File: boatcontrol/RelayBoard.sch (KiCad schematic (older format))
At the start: 15 parts, among them J2301 Conn_02x20_Odd_Even Header, J2302 TBL008V-1000-08BE, J2303 TBL008V-1000-08BE, K2301 EW60-1A3-CL12D04, K2302 EW60-1A3-CL12D04, K2303 EW60-1A3-CL12D04, K2304 EW60-1A3-CL12D04, K2305 EW60-1A3-CL12D04, K2306 EW60-1A3-CL12D04, K2307 EW60-1A3-CL12D04, K2308 EW60-1A3-CL12D04

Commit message: Organize more
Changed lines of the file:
@@
 AR Path="/E0EE2714/E107FCD3/E1098DA6" Ref="#PWR?"  Part="1"
 AR Path="/E171B338/E1098DA6" Ref="#PWR02301"  Part="1"
-AR Path="/E171B33C/5F80BAC6/E1098DA6" Ref="#PWR?"  Part="1"
-F 0 "#PWR?" H 3200 3800 50  0001 C CNN
+AR Path="/E171B33C/5F80BAC6/E1098DA6" Ref="#PWR0107"  Part="1"
+F 0 "#PWR0107" H 3200 3800 50  0001 C CNN
 F 1 "GND" H 3400 4050 50  0000 R CNN
 F 2 "" H 3200 4050 50  0001 C CNN
@@
 AR Path="/E0EE2714/E107FCD3/E1098DAC" Ref="#PWR?"  Part="1"
 AR Path="/E171B338/E1098DAC" Ref="#PWR02302"  Part="1"
-AR Path="/E171B33C/5F80BAC6/E1098DAC" Ref="#PWR?"  Part="1"
-F 0 "#PWR?" H 4250 3800 50  0001 C CNN
+AR Path="/E171B33C/5F80BAC6/E1098DAC" Ref="#PWR0123"  Part="1"
+F 0 "#PWR0123" H 4250 3800 50  0001 C CNN
 F 1 "GND" H 4450 4050 50  0000 R CNN
 F 2 "" H 4250 4050 50  0001 C CNN
@@
 AR Path="/E0EE2714/E107FCD3/E1098DB2" Ref="#PWR?"  Part="1"
 AR Path="/E171B338/E1098DB2" Ref="#PWR02303"  Part="1"
-AR Path="/E171B33C/5F80BAC6/E1098DB2" Ref="#PWR?"  Part="1"
-F 0 "#PWR?" H 5300 3800 50  0001 C CNN
+AR Path="/E171B33C/5F80BAC6/E1098DB2" Ref="#PWR0124"  Part="1"
+F 0 "#PWR0124" H 5300 3800 50  0001 C CNN
 F 1 "GND" H 5500 4050 50  0000 R CNN
 F 2 "" H 5300 4050 50  0001 C CNN
@@
 AR Path="/E0EE2714/E107FCD3/E1098DB8" Ref="#PWR?"  Part="1"
 AR Path="/E171B338/E1098DB8" Ref="#PWR02304"  Part="1"
-AR Path="/E171B33C/5F80BAC6/E1098DB8" Ref="#PWR?"  Part="1"
-F 0 "#PWR?" H 6350 3800 50  0001 C CNN
+AR Path="/E171B33C/5F80BAC6/E1098DB8" Ref="#PWR0125"  Part="1"
+F 0 "#PWR0125" H 6350 3800 50  0001 C CNN
 F 1 "GND" H 6550 4050 50  0000 R CNN
 F 2 "" H 6350 4050 50  0001 C CNN
@@
 AR Path="/E0EE2714/E107FCD3/E1098DC4" Ref="#PWR?"  Part="1"
 AR Path="/E171B338/E1098DC4" Ref="#PWR02306"  Part="1"
-AR Path="/E171B33C/5F80BAC6/E1098DC4" Ref="#PWR?"  Part="1"
-F 0 "#PWR?" H 8450 3800 50  0001 C CNN
+AR Path="/E171B33C/5F80BAC6/E1098DC4" Ref="#PWR0126"  Part="1"
+F 0 "#PWR0126" H 8450 3800 50  0001 C CNN
 F 1 "GND" H 8650 4050 50  0000 R CNN
 F 2 "" H 8450 4050 50  0001 C CNN
@@
 AR Path="/E0EE2714/E107FCD3/E1098DCA" Ref="#PWR?"  Part="1"
 AR Path="/E171B338/E1098DCA" Ref="#PWR02307"  Part="1"
-AR Path="/E171B33C/5F80BAC6/E1098DCA" Ref="#PWR?"  Part="1"
-F 0 "#PWR?" H 9500 3800 50  0001 C CNN
+AR Path="/E171B33C/5F80BAC6/E1098DCA" Ref="#PWR0127"  Part="1"
+F 0 "#PWR0127" H 9500 3800 50  0001 C CNN
 F 1 "GND" H 9700 4050 50  0000 R CNN
 F 2 "" H 9500 4050 50  0001 C CNN
@@
 AR Path="/E0EE2714/E107FCD3/E1098DD0" Ref="#PWR?"  Part="1"
 AR Path="/E171B338/E1098DD0" Ref="#PWR02308"  Part="1"
-AR Path="/E171B33C/5F80BAC6/E1098DD0" Ref="#PWR?"  Part="1"
-F 0 "#PWR?" H 10550 3800 50  0001 C CNN
+AR Path="/E171B33C/5F80BAC6/E1098DD0" Ref="#PWR0128"  Part="1"
+F 0 "#PWR0128" H 10550 3800 50  0001 C CNN
 F 1 "GND" H 10750 4050 50  0000 R CNN
 F 2 "" H 10550 4050 50  0001 C CNN
@@
 AR Path="/E0EE2714/E107FCD3/E1098DD9" Ref="J?"  Part="1"
 AR Path="/E171B338/E1098DD9" Ref="J2303"  Part="1"
-AR Path="/E171B33C/5F80BAC6/E1098DD9" Ref="J?"  Part="1"
-F 0 "J?" V 7146 4922 50  0000 R CNN
+AR Path="/E171B33C/5F80BAC6/E1098DD9" Ref="J3403"  Part="1"
+F 0 "J3403" V 7146 4922 50  0000 R CNN
 F 1 "TBL008V-1000-08BE" V 7400 5800 50  0000 R CNN
 F 2 "CUI_TBL008V-1000-08BE" H 7300 5350 50  0001 L BNN
@@
 AR Path="/E0EE2714/E107FCD3/E1098DE2" Ref="J?"  Part="1"
 AR Path="/E171B338/E1098DE2" Ref="J2302"  Part="1"
-AR Path="/E171B33C/5F80BAC6/E1098DE2" Ref="J?"  Part="1"
-F 0 "J?" V 7146 2372 50  0000 R CNN
+AR Path="/E171B33C/5F80BAC6/E1098DE2" Ref="J3402"  Part="1"
+F 0 "J3402" V 7146 2372 50  0000 R CNN
 F 1 "TBL008V-1000-08BE" V 7400 3250 50  0000 R CNN
 F 2 "CUI_TBL008V-1000-08BE" H 7300 2800 50  0001 L BNN
@@
 AR Path="/E0EE2714/E107FCD3/E1098DE8" Ref="K?"  Part="1"
 AR Path="/E171B338/E1098DE8" Ref="K2302"  Part="1"
-AR Path="/E171B33C/5F80BAC6/E1098DE8" Ref="K?"  Part="1"
-F 0 "K?" V 4800 3850 50  0000 L CNN
+AR Path="/E171B33C/5F80BAC6/E1098DE8" Ref="K3402"  Part="1"
+F 0 "K3402" V 4800 3850 50  0000 L CNN
 F 1 "EW60-1A3-CL12D04" V 4550 3600 50  0000 L CNN
 F 2 "BoatControl:TE_2071366-2" H 4750 4400 50  0001 L BNN
@@
 AR Path="/E0EE2714/E107FCD3/E1098DEE" Ref="K?"  Part="1"
 AR Path="/E171B338/E1098DEE" Ref="K2303"  Part="1"
-AR Path="/E171B33C/5F80BAC6/E1098DEE" Ref="K?"  Part="1"
-F 0 "K?" V 5850 3850 50  0000 L CNN
+AR Path="/E171B33C/5F80BAC6/E1098DEE" Ref="K3403"  Part="1"
+F 0 "K3403" V 5850 3850 50  0000 L CNN
 F 1 "EW60-1A3-CL12D04" V 5600 3600 50  0000 L CNN
 F 2 "BoatControl:TE_2071366-2" H 5800 4400 50  0001 L BNN
@@
 AR Path="/E0EE2714/E107FCD3/E1098DF4" Ref="K?"  Part="1"
 AR Path="/E171B338/E1098DF4" Ref="K2304"  Part="1"
-AR Path="/E171B33C/5F80BAC6/E1098DF4" Ref="K?"  Part="1"
-F 0 "K?" V 6900 3850 50  0000 L CNN
+AR Path="/E171B33C/5F80BAC6/E1098DF4" Ref="K3404"  Part="1"
+F 0 "K3404" V 6900 3850 50  0000 L CNN
 F 1 "EW60-1A3-CL12D04" V 6650 3600 50  0000 L CNN
 F 2 "BoatControl:TE_2071366-2" H 6850 4400 50  0001 L BNN
@@
 AR Path="/E0EE2714/E107FCD3/E1098DFA" Ref="K?"  Part="1"
 AR Path="/E171B338/E1098DFA" Ref="K2305"  Part="1"
-AR Path="/E171B33C/5F80BAC6/E1098DFA" Ref="K?"  Part="1"
-F 0 "K?" V 7950 3850 50  0000 L CNN
+AR Path="/E171B33C/5F80BAC6/E1098DFA" Ref="K3405"  Part="1"
+F 0 "K3405" V 7950 3850 50  0000 L CNN
 F 1 "EW60-1A3-CL12D04" V 7700 3600 50  0000 L CNN
 F 2 "BoatControl:TE_2071366-2" H 7900 4400 50  0001 L BNN
@@
 AR Path="/E0EE2714/E107FCD3/E1098E00" Ref="K?"  Part="1"
 AR Path="/E171B338/E1098E00" Ref="K2306"  Part="1"
-AR Path="/E171B33C/5F80BAC6/E1098E00" Ref="K?"  Part="1"
-F 0 "K?" V 9000 3850 50  0000 L CNN
+AR Path="/E171B33C/5F80BAC6/E1098E00" Ref="K3406"  Part="1"
+F 0 "K3406" V 9000 3850 50  0000 L CNN
 F 1 "EW60-1A3-CL12D04" V 8750 3600 50  0000 L CNN
 F 2 "BoatControl:TE_2071366-2" H 8950 4400 50  0001 L BNN
@@
 AR Path="/E0EE2714/E107FCD3/E1098E06" Ref="K?"  Part="1"
 AR Path="/E171B338/E1098E06" Ref="K2307"  Part="1"
-AR Path="/E171B33C/5F80BAC6/E1098E06" Ref="K?"  Part="1"
-F 0 "K?" V 10050 3850 50  0000 L CNN
+AR Path="/E171B33C/5F80BAC6/E1098E06" Ref="K3407"  Part="1"
+F 0 "K3407" V 10050 3850 50  0000 L CNN
 F 1 "EW60-1A3-CL12D04" V 9800 3600 50  0000 L CNN
 F 2 "BoatControl:TE_2071366-2" H 10000 4400 50  0001 L BNN
@@
 AR Path="/E0EE2714/E107FCD3/E1098E0C" Ref="K?"  Part="1"
 AR Path="/E171B338/E1098E0C" Ref="K2308"  Part="1"
-AR Path="/E171B33C/5F80BAC6/E1098E0C" Ref="K?"  Part="1"
-F 0 "K?" V 11100 3850 50  0000 L CNN
+AR Path="/E171B33C/5F80BAC6/E1098E0C" Ref="K3408"  Part="1"
+F 0 "K3408" V 11100 3850 50  0000 L CNN
 F 1 "EW60-1A3-CL12D04" V 10850 3550 50  0000 L CNN
 F 2 "BoatControl:TE_2071366-2" H 11050 4400 50  0001 L BNN
@@
 AR Path="/E0EE2714/E107FCD3/E1098E6E" Ref="J?"  Part="1"
 AR Path="/E171B338/E1098E6E" Ref="J2301"  Part="1"
-AR Path="/E171B33C/5F80BAC6/E1098E6E" Ref="J?"  Part="1"
-F 0 "J?" V 1346 2913 50  0000 R CNN
+AR Path="/E171B33C/5F80BAC6/E1098E6E" Ref="J3401"  Part="1"
+F 0 "J3401" V 1346 2913 50  0000 R CNN
 F 1 "Conn_02x20_Odd_Even Header" V 1300 4450 50  0000 R CNN
 F 2 "Connector_PinSocket_2.54mm:PinSocket_2x20_P2.54mm_Vertical" H 1250 4000 50  0001 C CNN
@@
 AR Path="/E0EE2714/E107FCD3/E1098E74" Ref="H?"  Part="1"
 AR Path="/E171B338/E1098E74" Ref="H2301"  Part="1"
-AR Path="/E171B33C/5F80BAC6/E1098E74" Ref="H?"  Part="1"
-F 0 "H?" H 150 3946 50  0000 L CNN
+AR Path="/E171B33C/5F80BAC6/E1098E74" Ref="H3401"  Part="1"
+F 0 "H3401" H 150 3946 50  0000 L CNN
 F 1 "MountingHole" H 150 3855 50  0000 L CNN
 F 2 "MountingHole:MountingHole_3mm" H 50  3900 50  0001 C CNN
@@
 AR Path="/E0EE2714/E107FCD3/E1098E7A" Ref="H?"  Part="1"
 AR Path="/E171B338/E1098E7A" Ref="H2302"  Part="1"
-AR Path="/E171B33C/5F80BAC6/E1098E7A" Ref="H?"  Part="1"
-F 0 "H?" H 150 4296 50  0000 L CNN
+AR Path="/E171B33C/5F80BAC6/E1098E7A" Ref="H3402"  Part="1"
+F 0 "H3402" H 150 4296 50  0000 L CNN
 F 1 "MountingHole" H 150 4205 50  0000 L CNN
 F 2 "MountingHole:MountingHole_3mm" H 50  4250 50  0001 C CNN
@@
 AR Path="/E0EE2714/E107FCD3/E1098E80" Ref="H?"  Part="1"
 AR Path="/E171B338/E1098E80" Ref="H2304"  Part="1"
-AR Path="/E171B33C/5F80BAC6/E1098E80" Ref="H?"  Part="1"
-F 0 "H?" H 2450 4296 50  0000 L CNN
+AR Path="/E171B33C/5F80BAC6/E1098E80" Ref="H3404"  Part="1"
+F 0 "H3404" H 2450 4296 50  0000 L CNN
 F 1 "MountingHole" H 2450 4205 50  0000 L CNN
 F 2 "MountingHole:MountingHole_3mm" H 2350 4250 50  0001 C CNN
@@
 AR Path="/E0EE2714/E107FCD3/E1098E86" Ref="H?"  Part="1"
 AR Path="/E171B338/E1098E86" Ref="H2303"  Part="1"
-AR Path="/E171B33C/5F80BAC6/E1098E86" Ref="H?"  Part="1"
-F 0 "H?" H 2450 3946 50  0000 L CNN
+AR Path="/E171B33C/5F80BAC6/E1098E86" Ref="H3403"  Part="1"
+F 0 "H3403" H 2450 3946 50  0000 L CNN
 F 1 "MountingHole" H 2450 3855 50  0000 L CNN
 F 2 "MountingHole:MountingHole_3mm" H 2350 3900 50  0001 C CNN
@@
 AR Path="/E0EE2714/E107FCD3/E1098E92" Ref="K?"  Part="1"
 AR Path="/E171B338/E1098E92" Ref="K2301"  Part="1"
-AR Path="/E171B33C/5F80BAC6/E1098E92" Ref="K?"  Part="1"
-F 0 "K?" V 3750 3850 50  0000 L CNN
+AR Path="/E171B33C/5F80BAC6/E1098E92" Ref="K3401"  Part="1"
+F 0 "K3401" V 3750 3850 50  0000 L CNN
 F 1 "EW60-1A3-CL12D04" V 3500 3600 50  0000 L CNN
 F 2 "BoatControl:TE_2071366-2" H 3700 4400 50  0001 L BNN
@@
 AR Path="/E0EE2714/E107FCD3/5F4F4DC8" Ref="#PWR?"  Part="1"
 AR Path="/E171B338/5F4F4DC8" Ref="#PWR02305"  Part="1"
-AR Path="/E171B33C/5F80BAC6/5F4F4DC8" Ref="#PWR?"  Part="1"
-F 0 "#PWR?" H 7400 3800 50  0001 C CNN
+AR Path="/E171B33C/5F80BAC6/5F4F4DC8" Ref="#PWR0129"  Part="1"
+F 0 "#PWR0129" H 7400 3800 50  0001 C CNN
 F 1 "GND" H 7600 4050 50  0000 R CNN
 F 2 "" H 7400 4050 50  0001 C CNN

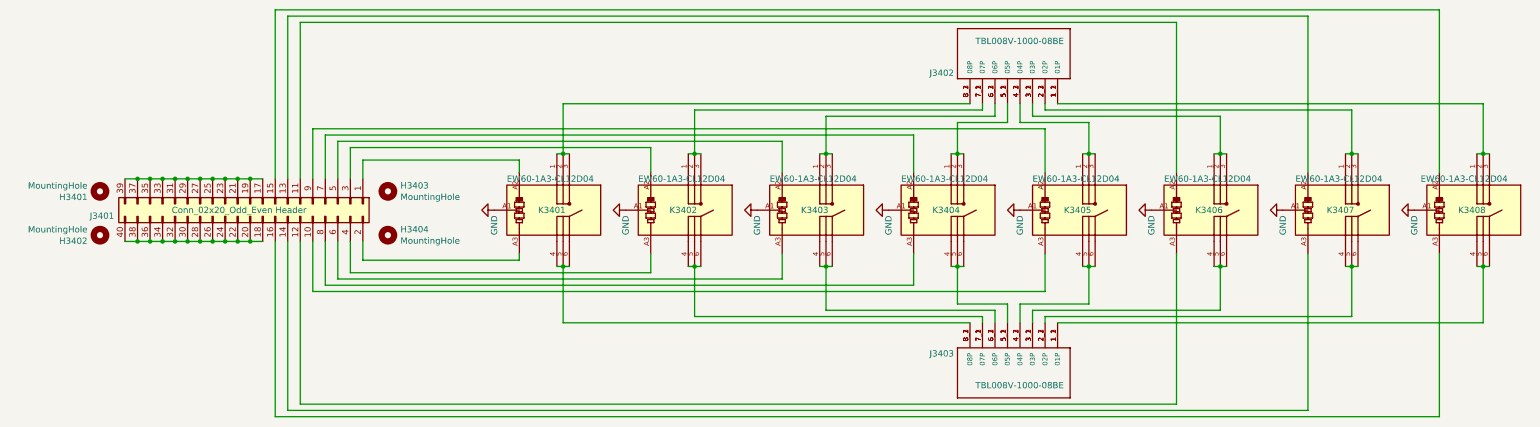
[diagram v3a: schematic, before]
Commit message: Restructure power and daughter boards
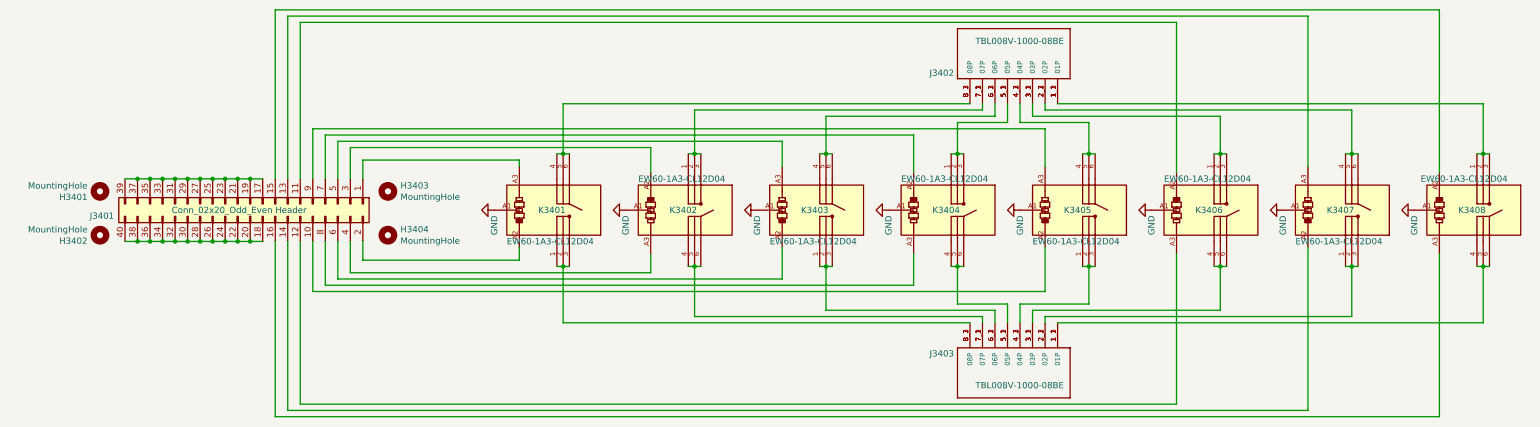
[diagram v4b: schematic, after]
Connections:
- net at J2303.2_1 (02P), J2303.2_2 (02P), J2303.2_3 (02P): now also K2307.1, K2307.2, K2307.3; no longer K2307.4, K2307.5, K2307.6
- net at J2303.4_1 (04P), J2303.4_2 (04P), J2303.4_3 (04P): now also K2305.1, K2305.2, K2305.3; no longer K2305.4, K2305.5, K2305.6
- net at J2303.6_1 (06P), J2303.6_2 (06P), J2303.6_3 (06P): now also K2303.1, K2303.2, K2303.3; no longer K2303.4, K2303.5, K2303.6
- net at J2303.8_1 (08P), J2303.8_2 (08P), J2303.8_3 (08P): now also K2301.1, K2301.2, K2301.3; no longer K2301.4, K2301.5, K2301.6
- net at J2302.2_1 (02P), J2302.2_2 (02P), J2302.2_3 (02P): now also K2307.4, K2307.5, K2307.6; no longer K2307.1, K2307.2, K2307.3
- net at J2302.4_1 (04P), J2302.4_2 (04P), J2302.4_3 (04P): now also K2305.4, K2305.5, K2305.6; no longer K2305.1, K2305.2, K2305.3
- net at J2302.6_1 (06P), J2302.6_2 (06P), J2302.6_3 (06P): now also K2303.4, K2303.5, K2303.6; no longer K2303.1, K2303.2, K2303.3
- net at J2302.8_1 (08P), J2302.8_2 (08P), J2302.8_3 (08P): now also K2301.4, K2301.5, K2301.6; no longer K2301.1, K2301.2, K2301.3
- net at K2303.A2: now also J2301.6 (Pin_6); no longer J2301.5 (Pin_5)
- net at K2303.A3: now also J2301.5 (Pin_5); no longer J2301.6 (Pin_6)
- net at K2305.A2: now also J2301.10 (Pin_10); no longer J2301.9 (Pin_9)
- net at K2305.A3: now also J2301.9 (Pin_9); no longer J2301.10 (Pin_10)
- net at K2307.A2: now also J2301.14 (Pin_14); no longer J2301.13 (Pin_13)
- net at K2307.A3: now also J2301.13 (Pin_13); no longer J2301.14 (Pin_14)
- net at J2301.1 (Pin_1): now also K2301.A3; no longer K2301.A2
- net at J2301.2 (Pin_2): now also K2301.A2; no longer K2301.A3

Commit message: Fixed daughter board
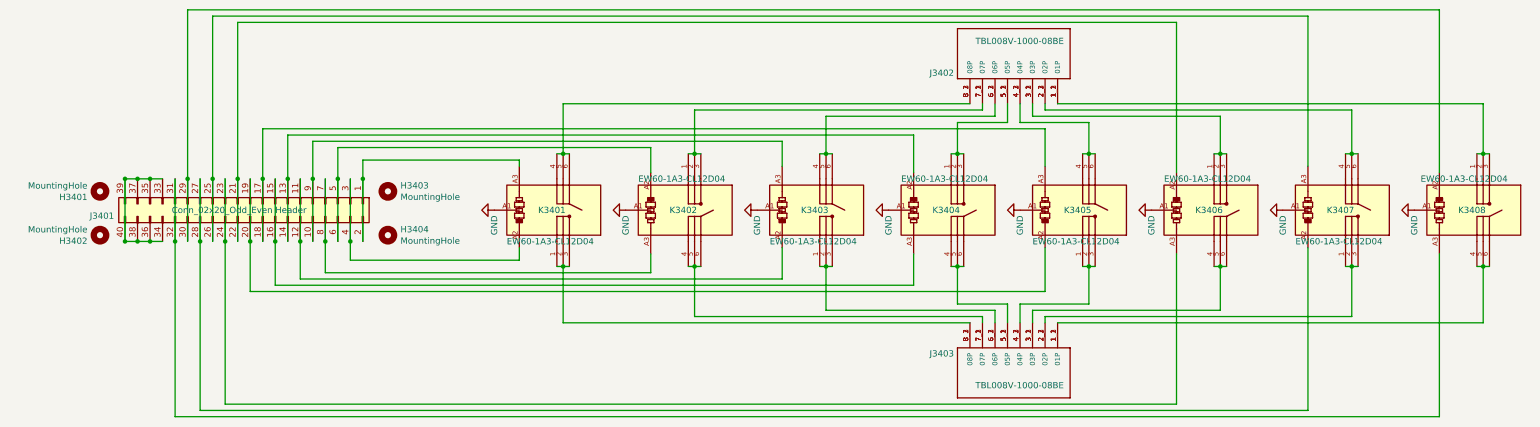
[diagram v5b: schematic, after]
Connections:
- net at K2302.A2: now also J2301.5 (Pin_5), J2301.6 (Pin_6); no longer J2301.3 (Pin_3)
- net at K2302.A3: now also J2301.7 (Pin_7), J2301.8 (Pin_8); no longer J2301.4 (Pin_4)
- net at K2303.A2: now also J2301.11 (Pin_11), J2301.12 (Pin_12); no longer J2301.6 (Pin_6)
- net at K2303.A3: now also J2301.10 (Pin_10), J2301.9 (Pin_9); no longer J2301.5 (Pin_5)
- net at K2304.A2: now also J2301.13 (Pin_13), J2301.14 (Pin_14); no longer J2301.7 (Pin_7)
- net at K2304.A3: now also J2301.15 (Pin_15), J2301.16 (Pin_16); no longer J2301.8 (Pin_8)
- net at K2305.A2: now also J2301.19 (Pin_19), J2301.20 (Pin_20); no longer J2301.10 (Pin_10)
- net at K2305.A3: now also J2301.17 (Pin_17), J2301.18 (Pin_18); no longer J2301.9 (Pin_9)
- net at K2306.A2: now also J2301.21 (Pin_21), J2301.22 (Pin_22); no longer J2301.11 (Pin_11)
- net at K2306.A3: now also J2301.23 (Pin_23), J2301.24 (Pin_24); no longer J2301.12 (Pin_12)
- net at K2307.A2: now also J2301.27 (Pin_27), J2301.28 (Pin_28); no longer J2301.14 (Pin_14)
- net at K2307.A3: now also J2301.25 (Pin_25), J2301.26 (Pin_26); no longer J2301.13 (Pin_13)
- net at K2308.A2: now also J2301.29 (Pin_29), J2301.30 (Pin_30); no longer J2301.15 (Pin_15)
- net at K2308.A3: now also J2301.31 (Pin_31), J2301.32 (Pin_32); no longer J2301.16 (Pin_16)
- net at J2301.1 (Pin_1), K2301.A3: now also J2301.2 (Pin_2)
- net at K2301.A2: now also J2301.3 (Pin_3), J2301.4 (Pin_4); no longer J2301.2 (Pin_2)
- new net: J2301.33 (Pin_33), J2301.34 (Pin_34), J2301.35 (Pin_35), J2301.36 (Pin_36), J2301.37 (Pin_37), J2301.38 (Pin_38), J2301.39 (Pin_39), J2301.40 (Pin_40)
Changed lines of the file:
@@
 Wire Wire Line
 	2150 3650 3400 3650
-Wire Wire Line
-	7600 3400 1750 3400
-Wire Wire Line
-	9700 2500 1550 2500
 $Comp
 L BoatControl:EW60-1A3-CL12D04 K?
@@
 	250  4300 350  4300
 Wire Wire Line
-	1250 4300 1350 4300
-Connection ~ 1250 4300
-Wire Wire Line
-	1150 4300 1250 4300
-Connection ~ 1150 4300
-Wire Wire Line
-	1050 4300 1150 4300
-Connection ~ 1050 4300
-Wire Wire Line
-	950  4300 1050 4300
-Connection ~ 950  4300
-Wire Wire Line
-	850  4300 950  4300
-Connection ~ 850  4300
-Wire Wire Line
-	750  4300 850  4300
-Connection ~ 750  4300
-Wire Wire Line
-	650  4300 750  4300
-Connection ~ 650  4300
-Wire Wire Line
-	550  4300 650  4300
-Connection ~ 550  4300
-Wire Wire Line
 	450  4300 550  4300
 Connection ~ 450  4300
 Wire Wire Line
-	1250 3800 1150 3800
-Connection ~ 1250 3800
-Wire Wire Line
-	1150 3800 1050 3800
-Connection ~ 1150 3800
-Wire Wire Line
-	1050 3800 950  3800
-Connection ~ 1050 3800
-Wire Wire Line
-	950  3800 850  3800
-Connection ~ 950  3800
-Wire Wire Line
-	850  3800 750  3800
-Connection ~ 850  3800
-Wire Wire Line
-	750  3800 650  3800
-Connection ~ 750  3800
-Wire Wire Line
-	650  3800 550  3800
-Connection ~ 650  3800
-Wire Wire Line
 	550  3800 450  3800
-Connection ~ 550  3800
 Wire Wire Line
 	450  3800 350  3800
@@
 	350  3800 250  3800
 Connection ~ 350  3800
-Wire Wire Line
-	1350 3800 1250 3800
 $Comp
 L Connector_Generic:Conn_02x20_Odd_Even J?
@@
 $EndComp
 Wire Wire Line
-	10750 2450 1450 2450
-Wire Wire Line
-	10750 5700 1450 5700
-Wire Wire Line
-	1550 5650 9700 5650
-Wire Wire Line
-	8650 2550 1650 2550
-Wire Wire Line
-	8650 5600 1650 5600
-Wire Wire Line
-	7600 4700 1750 4700
-Wire Wire Line
-	6550 3450 1850 3450
-Wire Wire Line
-	6550 4650 1850 4650
-Wire Wire Line
-	5500 4600 1950 4600
-Wire Wire Line
-	4450 3550 2050 3550
-Wire Wire Line
-	4450 4550 2050 4550
-Wire Wire Line
-	3400 4450 2150 4450
-Wire Wire Line
 	2150 3650 2150 3800
 Wire Wire Line
-	2050 3550 2050 3800
-Wire Wire Line
-	1950 3500 1950 3800
-Wire Wire Line
-	1850 3450 1850 3800
-Wire Wire Line
-	1750 3400 1750 3800
-Wire Wire Line
-	1650 2550 1650 3800
-Wire Wire Line
-	1550 2500 1550 3800
-Wire Wire Line
-	1450 3800 1450 2450
-Wire Wire Line
-	2150 4450 2150 4300
-Wire Wire Line
-	2050 4550 2050 4300
-Wire Wire Line
-	1950 4600 1950 4300
-Wire Wire Line
-	1850 4650 1850 4300
-Wire Wire Line
-	1750 4700 1750 4300
-Wire Wire Line
-	1650 5600 1650 4300
-Wire Wire Line
-	1550 4300 1550 5650
-Wire Wire Line
-	1450 5700 1450 4300
-Wire Wire Line
-	1950 3500 5500 3500
+	650  5700 650  4300
+Wire Wire Line
+	650  4300 650  3800
+Connection ~ 650  4300
+Wire Wire Line
+	750  2450 750  3800
+Wire Wire Line
+	750  3800 750  4300
+Connection ~ 750  3800
+Wire Wire Line
+	750  2450 10750 2450
+Wire Wire Line
+	650  5700 10750 5700
+Wire Wire Line
+	850  5650 850  4300
+Wire Wire Line
+	850  4300 850  3800
+Connection ~ 850  4300
+Wire Wire Line
+	850  5650 9700 5650
+Wire Wire Line
+	950  2500 950  3800
+Wire Wire Line
+	950  4300 950  3800
+Connection ~ 950  3800
+Wire Wire Line
+	950  2500 9700 2500
+Wire Wire Line
+	1050 4300 1050 5600
+Wire Wire Line
+	1050 4300 1050 3800
+Connection ~ 1050 4300
+Wire Wire Line
+	1050 5600 8650 5600
+Wire Wire Line
+	1150 3800 1150 2550
+Wire Wire Line
+	1150 2550 8650 2550
+Wire Wire Line
+	1250 4700 1250 4300
+Wire Wire Line
+	1250 4300 1250 3800
+Connection ~ 1250 4300
+Wire Wire Line
+	1150 4300 1150 3800
+Connection ~ 1150 3800
+Wire Wire Line
+	1250 4700 7600 4700
+Wire Wire Line
+	1350 3400 1350 3800
+Wire Wire Line
+	1350 4300 1350 3800
+Connection ~ 1350 3800
+Wire Wire Line
+	1350 3400 7600 3400
+Wire Wire Line
+	1450 4650 1450 4300
+Wire Wire Line
+	1450 4300 1450 3800
+Connection ~ 1450 4300
+Wire Wire Line
+	1450 4650 6550 4650
+Wire Wire Line
+	1550 3450 1550 3800
+Wire Wire Line
+	1550 4300 1550 3800
+Connection ~ 1550 3800
+Wire Wire Line
+	1550 3450 6550 3450
+Wire Wire Line
+	1650 4600 1650 4300
+Wire Wire Line
+	1650 4300 1650 3800
+Connection ~ 1650 4300
+Wire Wire Line
+	1650 4600 5500 4600
+Wire Wire Line
+	1750 3500 1750 3800
+Wire Wire Line
+	1750 3800 1750 4300
+Connection ~ 1750 3800
+Wire Wire Line
+	1750 3500 5500 3500
+Wire Wire Line
+	1850 4550 1850 4300
+Wire Wire Line
+	1850 4300 1850 3800
+Connection ~ 1850 4300
+Wire Wire Line
+	1850 4550 4450 4550
+Wire Wire Line
+	1950 3550 1950 3800
+Wire Wire Line
+	1950 3800 1950 4300
+Connection ~ 1950 3800
+Wire Wire Line
+	1950 3550 4450 3550
+Wire Wire Line
+	2050 4450 2050 4300
+Wire Wire Line
+	2050 4300 2050 3800
+Connection ~ 2050 4300
+Wire Wire Line
+	2050 4450 3400 4450
+Wire Wire Line
+	2150 3800 2150 4300
+Connection ~ 2150 3800
+Wire Wire Line
+	250  3800 250  4300
+Connection ~ 250  3800
+Connection ~ 250  4300
 $EndSCHEMATC
